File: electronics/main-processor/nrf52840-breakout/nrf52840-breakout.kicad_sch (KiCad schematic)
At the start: 78 parts, among them J1 TBP02R2-381-03BE, J2 TBP02R2-381-02BE, J3 ST1W008S4AR1500, J4 TBP02R2-381-03BE, J5 USB4070-30-C_REVC5, J6 CONUFL001-SMD-T, J7 21992304, J8 Conn_01x04_Male, J9 TBP02R2-381-02BE, Q1 BSS214NW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

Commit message: finalised board routing for first prototype
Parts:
- removed R23: 20K, Resistor_SMD:R_0805_2012Metric, symbol Device:R
- removed R24: 10K, Resistor_SMD:R_0805_2012Metric, symbol Device:R
- J5: footprint USB4070-30-C:USB4070-30-C -> GCT_USB4070-30-C_REVC5
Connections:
- net at J5.B1 (GND_B): no longer J5.B12 (GND_B)
- net at J5.B4 (VBUS_B): no longer J5.B9 (VBUS_B)
- no-connect marks 28 -> 30
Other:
- moved on the sheet: R14
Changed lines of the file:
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@@
   (junction (at 226.822 40.64) (diameter 0) (color 0 0 0 0)
   )
-  (junction (at 110.617 258.572) (diameter 0) (color 0 0 0 0)
-  )
   (junction (at 186.182 81.28) (diameter 0) (color 0 0 0 0)
   )
@@
   (no_connect (at 245.237 152.019))
   (no_connect (at 245.237 134.239))
+  (no_connect (at 66.167 159.639))
+  (no_connect (at 66.167 157.099))
   (no_connect (at 137.414 218.186))
   (no_connect (at 137.414 220.726))
@@
   (no_connect (at 162.814 246.126))
   (no_connect (at 156.972 83.82))
+  (no_connect (at 66.167 146.939))
   (no_connect (at 30.607 146.939))
   (no_connect (at 30.607 149.479))
@@
   (no_connect (at 66.167 134.239))
   (no_connect (at 66.167 136.779))
-  (no_connect (at 66.167 149.479))
   (no_connect (at 66.167 152.019))
   (no_connect (at 66.167 154.559))
@@
     (stroke (width 0) (type default) (color 0 0 0 0))
   )
-  (wire (pts (xy 109.347 258.572) (xy 110.617 258.572))
-    (stroke (width 0) (type default) (color 0 0 0 0))
-  )
   (wire (pts (xy 280.416 165.354) (xy 282.194 165.354))
     (stroke (width 0) (type default) (color 0 0 0 0))
@@
     (stroke (width 0) (type default) (color 0 0 0 0))
   )
-  (wire (pts (xy 110.617 258.572) (xy 110.617 260.731))
-    (stroke (width 0) (type default) (color 0 0 0 0))
-  )
   (polyline (pts (xy 341.63 102.997) (xy 341.63 130.429))
     (stroke (width 0) (type default) (color 0 0 0 0))
@@
     (stroke (width 0) (type default) (color 0 0 0 0))
   )
-  (wire (pts (xy 110.617 256.286) (xy 110.617 258.572))
-    (stroke (width 0) (type default) (color 0 0 0 0))
-  )
   (wire (pts (xy 111.633 154.432) (xy 111.633 151.892))
     (stroke (width 0) (type default) (color 0 0 0 0))
@@
     )
   )
-  (global_label "BATT_VIN{slash}3" (shape input) (at 109.347 258.572 180) (fields_autoplaced)
-    (effects (font (size 1.27 1.27)) (justify right))
-    (property "Intersheet References" "${INTERSHEET_REFS}" (id 0) (at 96.1087 258.4926 0)
-      (effects (font (size 1.27 1.27)) (justify right) hide)
-    )
-  )
   (global_label "GPIO0" (shape input) (at 162.814 223.266 0) (fields_autoplaced)
     (effects (font (size 1.27 1.27)) (justify left))
@@
     (pin "2")
   )
-  (symbol (lib_id "power:VBUS") (at 110.617 248.666 0) (unit 1)
-    (in_bom yes) (on_board yes)
-    (property "Reference" "#PWR0135" (id 0) (at 110.617 252.476 0)
-      (effects (font (size 1.27 1.27)) hide)
-    )
-    (property "Value" "VBUS" (id 1) (at 113.157 245.237 0)
-      (effects (font (size 1.27 1.27)) (justify right))
-    )
-    (property "Footprint" "" (id 2) (at 110.617 248.666 0)
-      (effects (font (size 1.27 1.27)) hide)
-    )
-    (property "Datasheet" "" (id 3) (at 110.617 248.666 0)
-      (effects (font (size 1.27 1.27)) hide)
-    )
-    (pin "1")
-  )
   (symbol (lib_id "power:GND") (at 197.485 256.54 0) (unit 1)
     (in_bom yes) (on_board yes) (fields_autoplaced)
@@
     (pin "5")
   )
-  (symbol (lib_id "power:GND") (at 110.617 268.351 0) (unit 1)
-    (in_bom yes) (on_board yes) (fields_autoplaced)
-    (property "Reference" "#PWR0139" (id 0) (at 110.617 274.701 0)
-      (effects (font (size 1.27 1.27)) hide)
-    )
-    (property "Value" "GND" (id 1) (at 110.617 272.7944 0))
-    (property "Footprint" "" (id 2) (at 110.617 268.351 0)
-      (effects (font (size 1.27 1.27)) hide)
-    )
-    (property "Datasheet" "" (id 3) (at 110.617 268.351 0)
-      (effects (font (size 1.27 1.27)) hide)
-    )
-    (pin "1")
-  )
   (symbol (lib_id "Device:R") (at 106.553 77.216 0) (unit 1)
     (in_bom yes) (on_board yes) (fields_autoplaced)
@@
     (pin "2")
   )
-  (symbol (lib_id "Device:R") (at 110.617 252.476 0) (unit 1)
-    (in_bom yes) (on_board yes) (fields_autoplaced)
-    (property "Reference" "R23" (id 0) (at 112.395 251.6413 0)
-      (effects (font (size 1.27 1.27)) (justify left))
-    )
-    (property "Value" "20K" (id 1) (at 112.395 254.1782 0)
-      (effects (font (size 1.27 1.27)) (justify left))
-    )
-    (property "Footprint" "Resistor_SMD:R_0805_2012Metric" (id 2) (at 108.839 252.476 90)
-      (effects (font (size 1.27 1.27)) hide)
-    )
-    (property "Datasheet" "~" (id 3) (at 110.617 252.476 0)
-      (effects (font (size 1.27 1.27)) hide)
-    )
-    (pin "1")
-    (pin "2")
-  )
   (symbol (lib_id "CBC2518T100M:CBC2518T100M") (at 325.374 56.642 0) (unit 1)
     (in_bom yes) (on_board yes) (fields_autoplaced)
@@
     (pin "2")
   )
-  (symbol (lib_id "Device:R") (at 69.977 146.939 270) (unit 1)
+  (symbol (lib_id "Device:R") (at 69.977 149.479 270) (unit 1)
     (in_bom yes) (on_board yes) (fields_autoplaced)
-    (property "Reference" "R14" (id 0) (at 69.977 142.2232 90))
-    (property "Value" "5.1K" (id 1) (at 69.977 144.7601 90))
-    (property "Footprint" "Resistor_SMD:R_0805_2012Metric" (id 2) (at 69.977 145.161 90)
+    (property "Reference" "R14" (id 0) (at 69.977 144.7632 90))
+    (property "Value" "5.1K" (id 1) (at 69.977 147.3001 90))
+    (property "Footprint" "Resistor_SMD:R_0805_2012Metric" (id 2) (at 69.977 147.701 90)
       (effects (font (size 1.27 1.27)) hide)
     )
-    (property "Datasheet" "~" (id 3) (at 69.977 146.939 0)
+    (property "Datasheet" "~" (id 3) (at 69.977 149.479 0)
       (effects (font (size 1.27 1.27)) hide)
     )
@@
     (pin "3")
   )
-  (symbol (lib_id "Device:R") (at 110.617 264.541 0) (unit 1)
-    (in_bom yes) (on_board yes) (fields_autoplaced)
-    (property "Reference" "R24" (id 0) (at 112.395 263.7063 0)
-      (effects (font (size 1.27 1.27)) (justify left))
-    )
-    (property "Value" "10K" (id 1) (at 112.395 266.2432 0)
-      (effects (font (size 1.27 1.27)) (justify left))
-    )
-    (property "Footprint" "Resistor_SMD:R_0805_2012Metric" (id 2) (at 108.839 264.541 90)
-      (effects (font (size 1.27 1.27)) hide)
-    )
-    (property "Datasheet" "~" (id 3) (at 110.617 264.541 0)
-      (effects (font (size 1.27 1.27)) hide)
-    )
-    (pin "1")
-    (pin "2")
-  )
   (symbol (lib_id "power:GND") (at 64.262 86.36 0) (unit 1)
     (in_bom yes) (on_board yes) (fields_autoplaced)
@@
     (pin "8")
   )
+  (symbol (lib_id "power:GND") (at 30.607 157.099 270) (unit 1)
+    (in_bom yes) (on_board yes)
+    (property "Reference" "#PWR0135" (id 0) (at 24.257 157.099 0)
+      (effects (font (size 1.27 1.27)) hide)
+    )
+    (property "Value" "GND" (id 1) (at 23.241 157.099 90)
+      (effects (font (size 1.27 1.27)) (justify left))
+    )
+    (property "Footprint" "" (id 2) (at 30.607 157.099 0)
+      (effects (font (size 1.27 1.27)) hide)
+    )
+    (property "Datasheet" "" (id 3) (at 30.607 157.099 0)
+      (effects (font (size 1.27 1.27)) hide)
+    )
+    (pin "1")
+  )
   (symbol (lib_id "power:GND") (at 212.852 86.36 0) (unit 1)
     (in_bom yes) (on_board yes) (fields_autoplaced)
@@
     (pin "2")
   )
-  (symbol (lib_id "power:GND") (at 73.787 146.939 90) (unit 1)
+  (symbol (lib_id "power:GND") (at 73.787 149.479 90) (unit 1)
     (in_bom yes) (on_board yes)
-    (property "Reference" "#PWR0108" (id 0) (at 80.137 146.939 0)
+    (property "Reference" "#PWR0108" (id 0) (at 80.137 149.479 0)
       (effects (font (size 1.27 1.27)) hide)
     )
-    (property "Value" "GND" (id 1) (at 81.153 146.939 90)
+    (property "Value" "GND" (id 1) (at 81.153 149.479 90)
       (effects (font (size 1.27 1.27)) (justify left))
     )
-    (property "Footprint" "" (id 2) (at 73.787 146.939 0)
+    (property "Footprint" "" (id 2) (at 73.787 149.479 0)
       (effects (font (size 1.27 1.27)) hide)
     )
-    (property "Datasheet" "" (id 3) (at 73.787 146.939 0)
+    (property "Datasheet" "" (id 3) (at 73.787 149.479 0)
       (effects (font (size 1.27 1.27)) hide)
     )
@@
     (property "Reference" "J5" (id 0) (at 48.387 125.4592 0))
     (property "Value" "USB4070-30-C_REVC5" (id 1) (at 48.387 127.9961 0))
-    (property "Footprint" "USB4070-30-C:USB4070-30-C" (id 2) (at 48.387 144.399 0)
+    (property "Footprint" "GCT_USB4070-30-C_REVC5" (id 2) (at 48.387 148.209 0)
       (effects (font (size 1.27 1.27)) (justify left bottom) hide)
     )
@@
       (effects (font (size 1.27 1.27)) (justify left bottom) hide)
     )
-    (property "STANDARD" "Manufacturer Recommendations" (id 7) (at 48.387 144.399 0)
+    (property "STANDARD" "Manufacturer Recommendations" (id 7) (at 48.387 148.209 0)
       (effects (font (size 1.27 1.27)) (justify left bottom) hide)
     )
@@
       (reference "#PWR0134") (unit 1) (value "+3.3V") (footprint "")
     )
-    (path "/3191d128-6b15-4702-bf2c-988adf8e38a4"
-      (reference "#PWR0135") (unit 1) (value "VBUS") (footprint "")
+    (path "/c8cb8481-0a9c-44b2-a168-1d72fc105c4e"
+      (reference "#PWR0135") (unit 1) (value "GND") (footprint "")
     )
     (path "/e8201a46-5719-43f6-bf22-4551b211ba3f"
@@
       (reference "#PWR0138") (unit 1) (value "GND") (footprint "")
     )
-    (path "/99473000-4a10-438a-b0c3-09d26ccc9608"
-      (reference "#PWR0139") (unit 1) (value "GND") (footprint "")
-    )
     (path "/73e07c4b-d44e-425a-9132-b21969f7b2d5"
       (reference "#PWR0140") (unit 1) (value "GND") (footprint "")
@@
     )
     (path "/fbacf336-f127-47e8-8215-e93e0a16f9a1"
-      (reference "J5") (unit 1) (value "USB4070-30-C_REVC5") (footprint "USB4070-30-C:USB4070-30-C")
+      (reference "J5") (unit 1) (value "USB4070-30-C_REVC5") (footprint "GCT_USB4070-30-C_REVC5")
     )
     (path "/3b7e321c-e2ab-4e11-bafe-ee95a4ef18f3"
@@
       (reference "R22") (unit 1) (value "4.7K") (footprint "Resistor_SMD:R_0805_2012Metric")
     )
-    (path "/b3c7cb4d-12ed-4515-940d-cc06ee2617aa"
-      (reference "R23") (unit 1) (value "20K") (footprint "Resistor_SMD:R_0805_2012Metric")
-    )
-    (path "/c25f03c0-f6ed-4b1e-b393-192bd3e0f817"
-      (reference "R24") (unit 1) (value "10K") (footprint "Resistor_SMD:R_0805_2012Metric")
-    )
     (path "/7e42edb0-9784-42d6-91f5-f690882afa89"

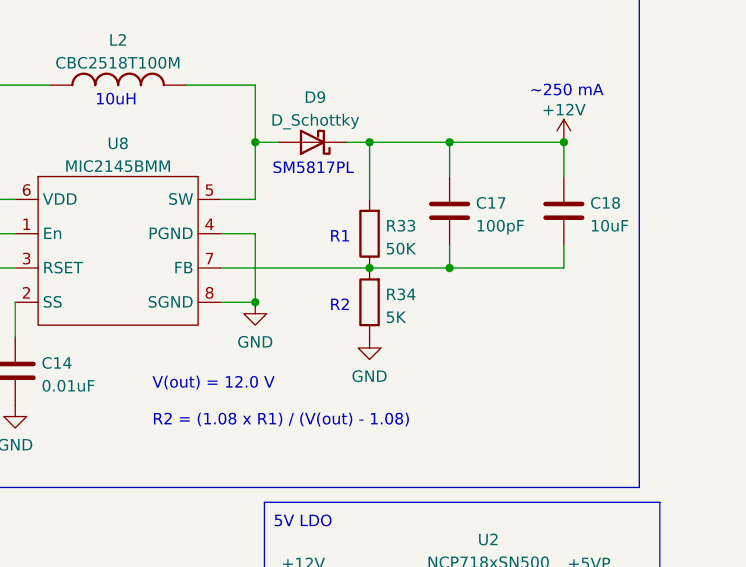
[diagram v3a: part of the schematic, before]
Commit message: added basic feather m0 node. Features: no solar, d-cell battery, 12 V boost, sd-card, SDI12, i2c, wind speed and dir, reverse polarity protection and indicator
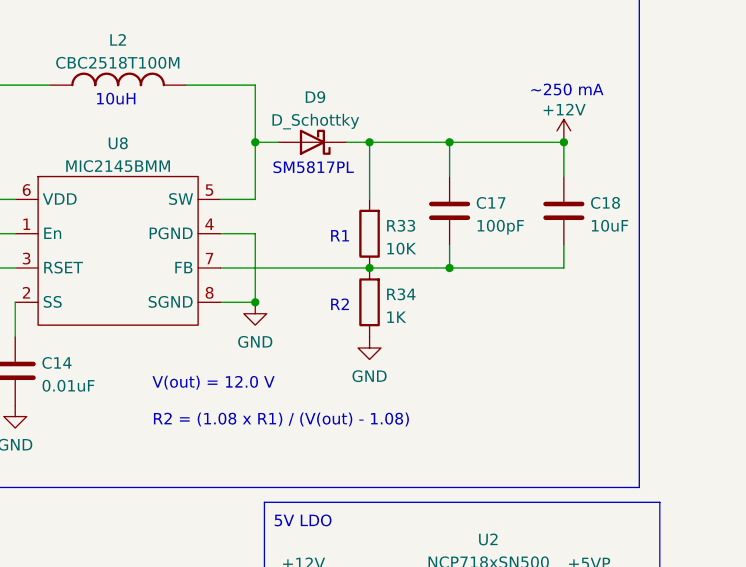
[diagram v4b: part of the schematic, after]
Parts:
- R33: value 50K -> 10K
- R34: value 5K -> 1K
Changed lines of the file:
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@@
       (effects (font (size 1.27 1.27)) (justify right))
     )
-    (property "Value" "5K" (id 1) (at 355.092 82.4742 0)
+    (property "Value" "1K" (id 1) (at 355.092 82.4742 0)
       (effects (font (size 1.27 1.27)) (justify right))
     )
@@
       (effects (font (size 1.27 1.27)) (justify right))
     )
-    (property "Value" "50K" (id 1) (at 355.092 74.8542 0)
+    (property "Value" "10K" (id 1) (at 355.092 74.8542 0)
       (effects (font (size 1.27 1.27)) (justify right))
     )
@@
     )
     (path "/4accf16d-a25f-493b-91ac-83bc1f3fee2e"
-      (reference "R33") (unit 1) (value "50K") (footprint "Resistor_SMD:R_0805_2012Metric")
+      (reference "R33") (unit 1) (value "10K") (footprint "Resistor_SMD:R_0805_2012Metric")
     )
     (path "/0cc9c345-cca3-4aa9-9cf9-f7a518168c7a"
-      (reference "R34") (unit 1) (value "5K") (footprint "Resistor_SMD:R_0805_2012Metric")
+      (reference "R34") (unit 1) (value "1K") (footprint "Resistor_SMD:R_0805_2012Metric")
     )
     (path "/0351f498-162f-4b0b-9bb8-4fe4dbccb3a1"

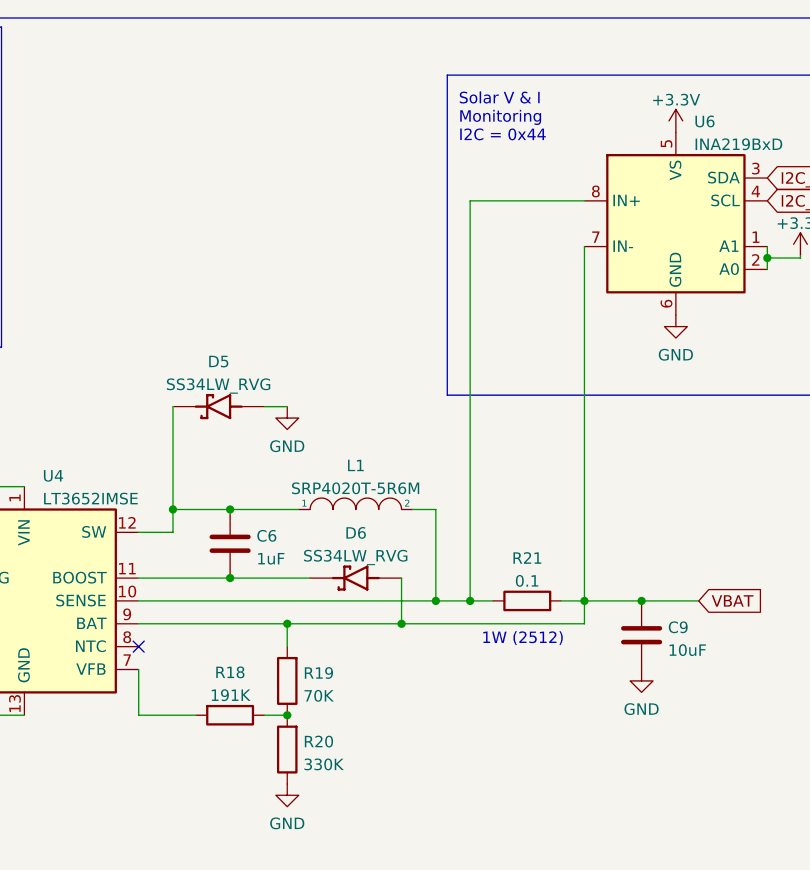
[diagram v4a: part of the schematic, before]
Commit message: initial commit of NRF52840 firmware testing
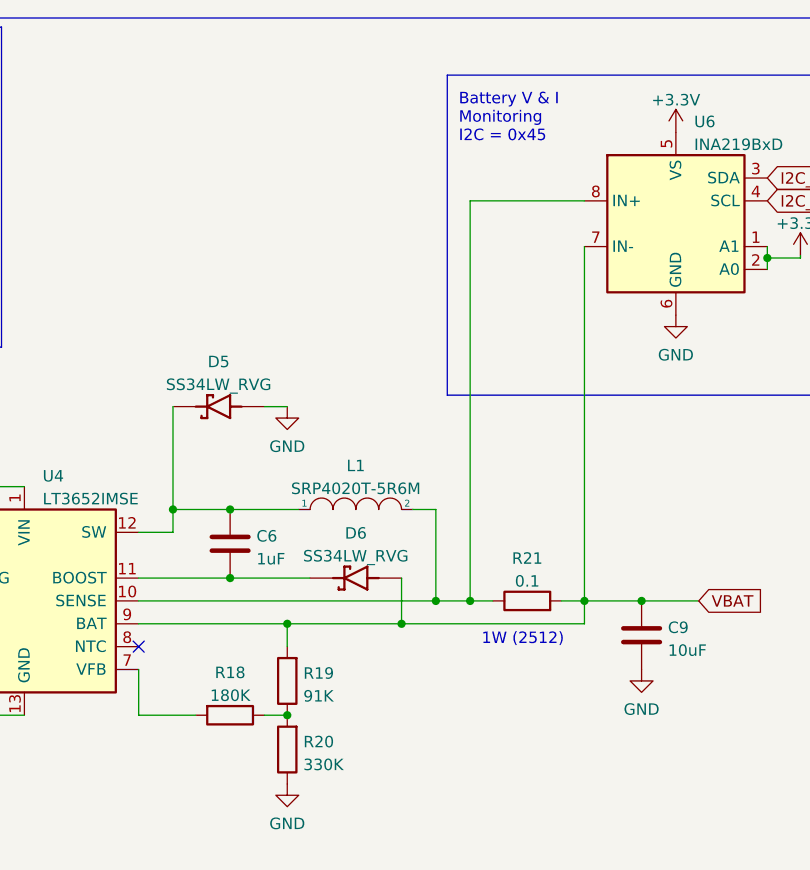
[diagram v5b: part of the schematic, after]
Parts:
- R18: value 191K -> 180K
- R19: value 70K -> 91K
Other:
- note added: "Battery V & I Monitoring I2C = 0x45"
- note removed: "Solar V & I Monitoring I2C = 0x44"
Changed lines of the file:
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@@
     (effects (font (size 1.27 1.27)) (justify left bottom))
   )
-  (text "Solar V & I\nMonitoring\nI2C = 0x44" (at 192.532 27.94 0)
+  (text "Battery V & I\nMonitoring\nI2C = 0x45" (at 192.532 27.94 0)
     (effects (font (size 1.27 1.27)) (justify left bottom))
   )
@@
     (in_bom yes) (on_board yes) (fields_autoplaced)
     (property "Reference" "R18" (id 0) (at 167.132 86.7242 90))
-    (property "Value" "191K" (id 1) (at 167.132 89.2611 90))
+    (property "Value" "180K" (id 1) (at 167.132 89.2611 90))
     (property "Footprint" "Resistor_SMD:R_0805_2012Metric" (id 2) (at 167.132 89.662 90)
       (effects (font (size 1.27 1.27)) hide)
@@
       (effects (font (size 1.27 1.27)) (justify right))
     )
-    (property "Value" "70K" (id 1) (at 175.26 89.3322 0)
+    (property "Value" "91K" (id 1) (at 175.26 89.3322 0)
       (effects (font (size 1.27 1.27)) (justify right))
     )
@@
     )
     (path "/cacee8e9-423b-4968-862b-184d8be6b9cf"
-      (reference "R18") (unit 1) (value "191K") (footprint "Resistor_SMD:R_0805_2012Metric")
+      (reference "R18") (unit 1) (value "180K") (footprint "Resistor_SMD:R_0805_2012Metric")
     )
     (path "/e1d5f52a-cb64-421f-a75a-7924dee02e38"
-      (reference "R19") (unit 1) (value "70K") (footprint "Resistor_SMD:R_0805_2012Metric")
+      (reference "R19") (unit 1) (value "91K") (footprint "Resistor_SMD:R_0805_2012Metric")
     )
     (path "/8cf41fbf-9a1b-4663-b37c-09cb6e01a4e7"
